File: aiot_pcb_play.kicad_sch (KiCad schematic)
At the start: 10 parts, among them J1 10_pin_swd_connector, J2 Tag-Connect, U1 BC833M, U2 16_pin_header, U3 ITM-DYPA-B-02

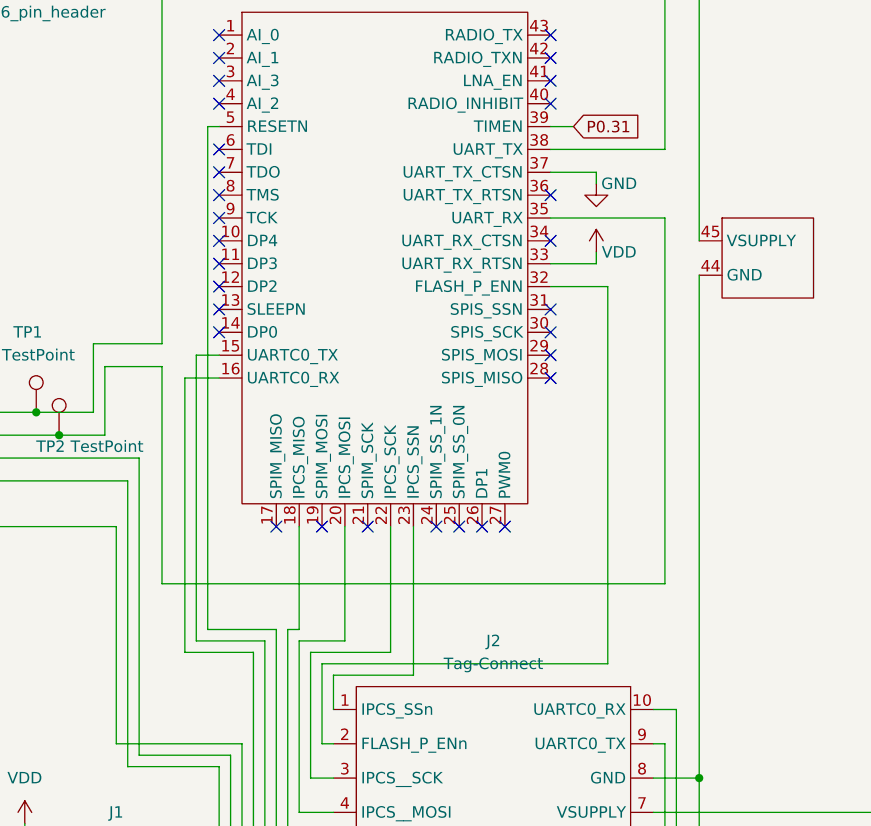
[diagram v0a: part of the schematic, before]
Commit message: Finished the design of the AIOT Play v1.2 addressing #5 and #6
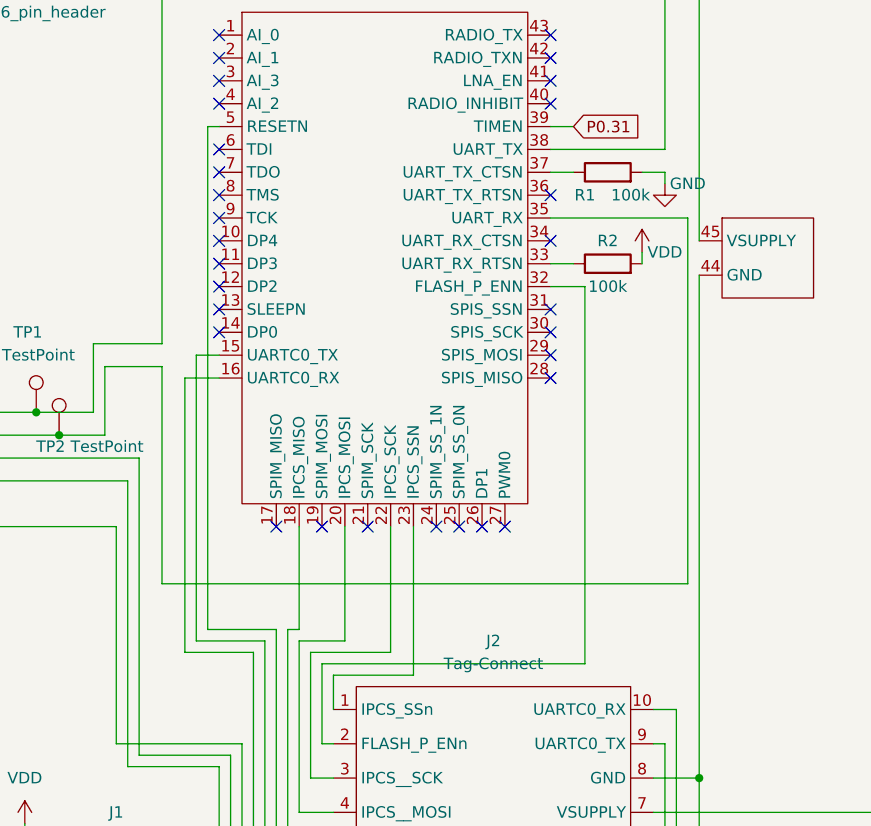
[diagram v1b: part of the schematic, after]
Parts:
- added R1, R2: 100k, Resistor_SMD:R_0603_1608Metric, symbol Device:R
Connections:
- net GND: now also R1.2; no longer U3.37 (UART_TX_CTSN)
- net VDD: now also R2.2; no longer U3.33 (UART_RX_RTSN)
- new net: R1.1, U3.37 (UART_TX_CTSN)
- new net: R2.1, U3.33 (UART_RX_RTSN)
